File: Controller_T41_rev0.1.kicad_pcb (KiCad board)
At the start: 2 copper layers, 79 x 119.8 mm, 19 parts, among them J1 RJ45_LED_Shielded_x2, J2 RJ45_LED_Shielded_x2, J3 RJ45_LED_Shielded_x2, J4 RJ45_LED_Shielded_x2, J9 Screw_Terminal_01x02, U1 74HC245, U2 74HC245, U3 Teensy4.1, U4 74HC245, U5 74HC245

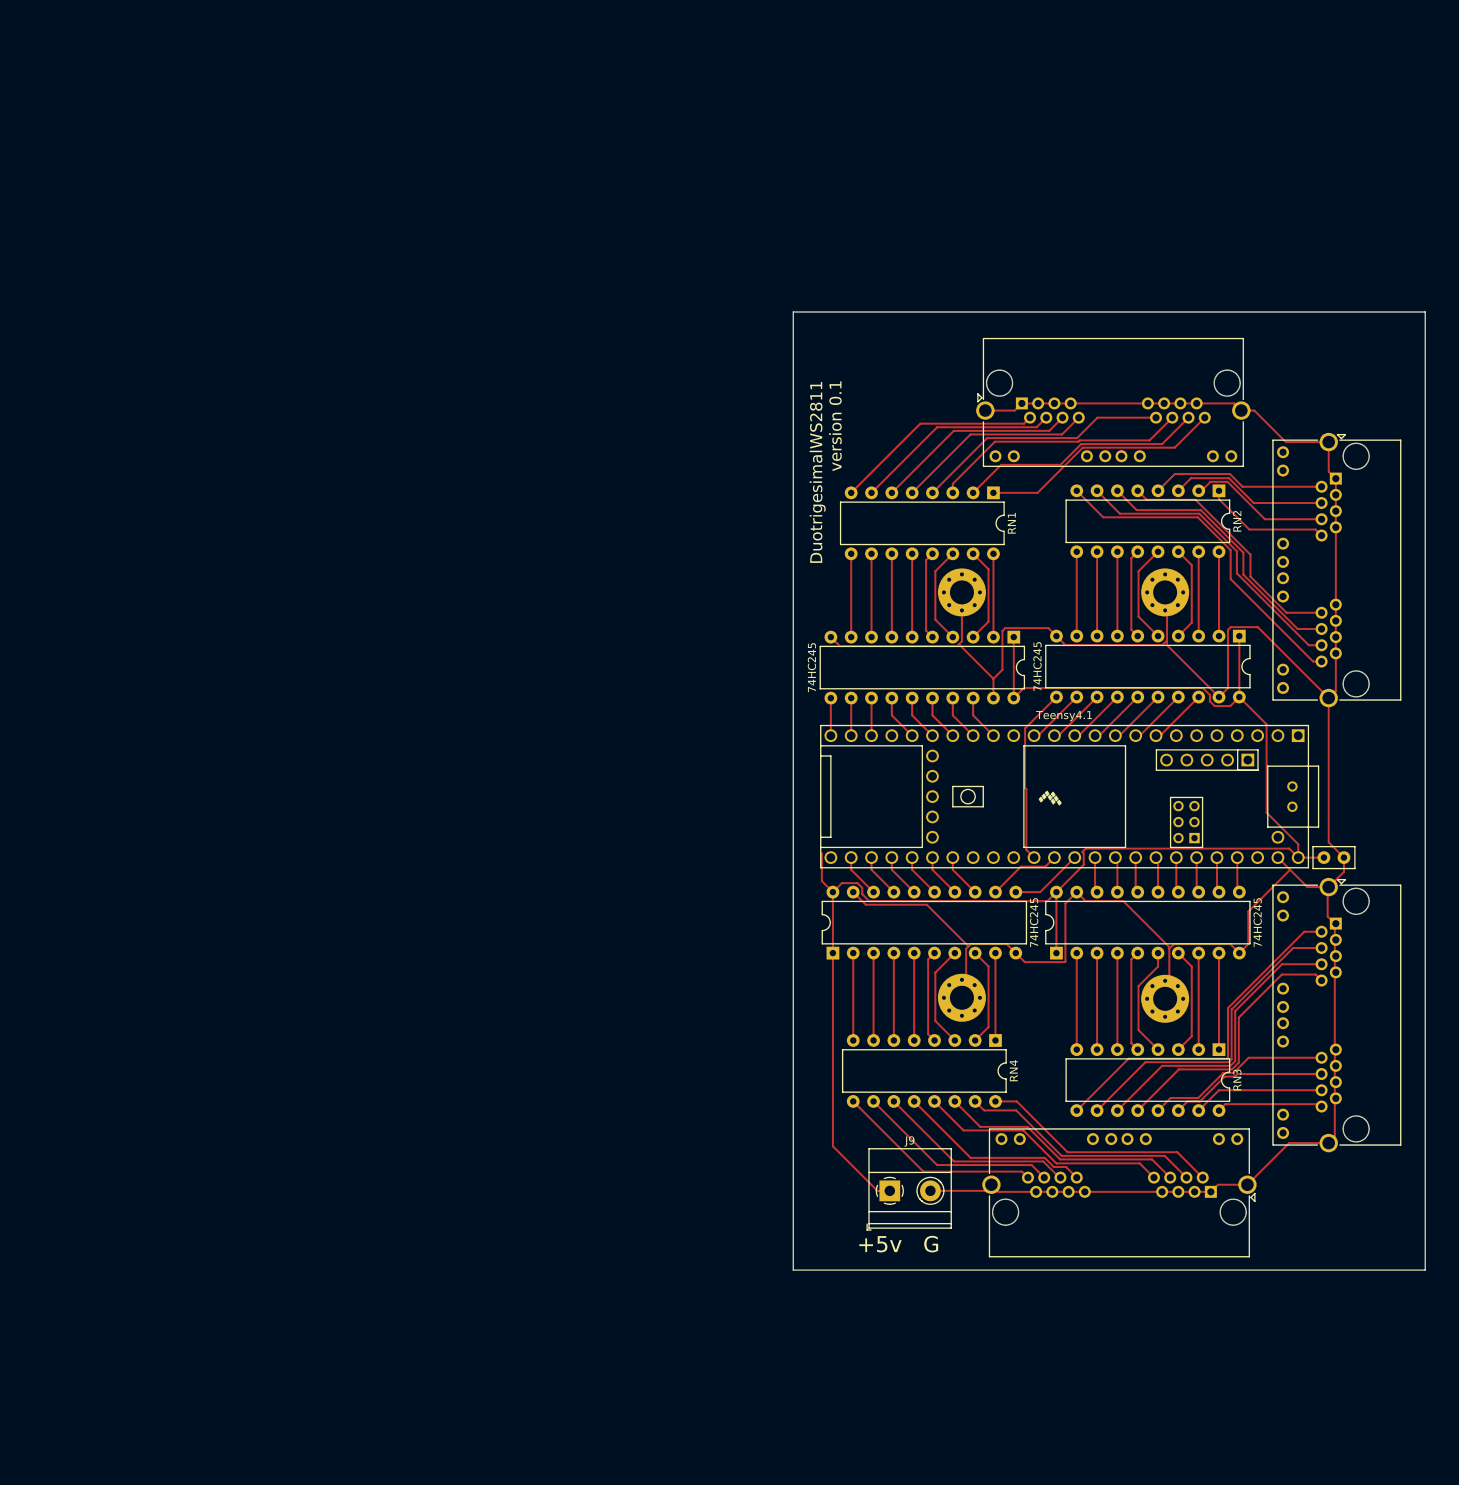
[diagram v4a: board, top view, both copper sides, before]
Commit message: Switching to SMT components where possible
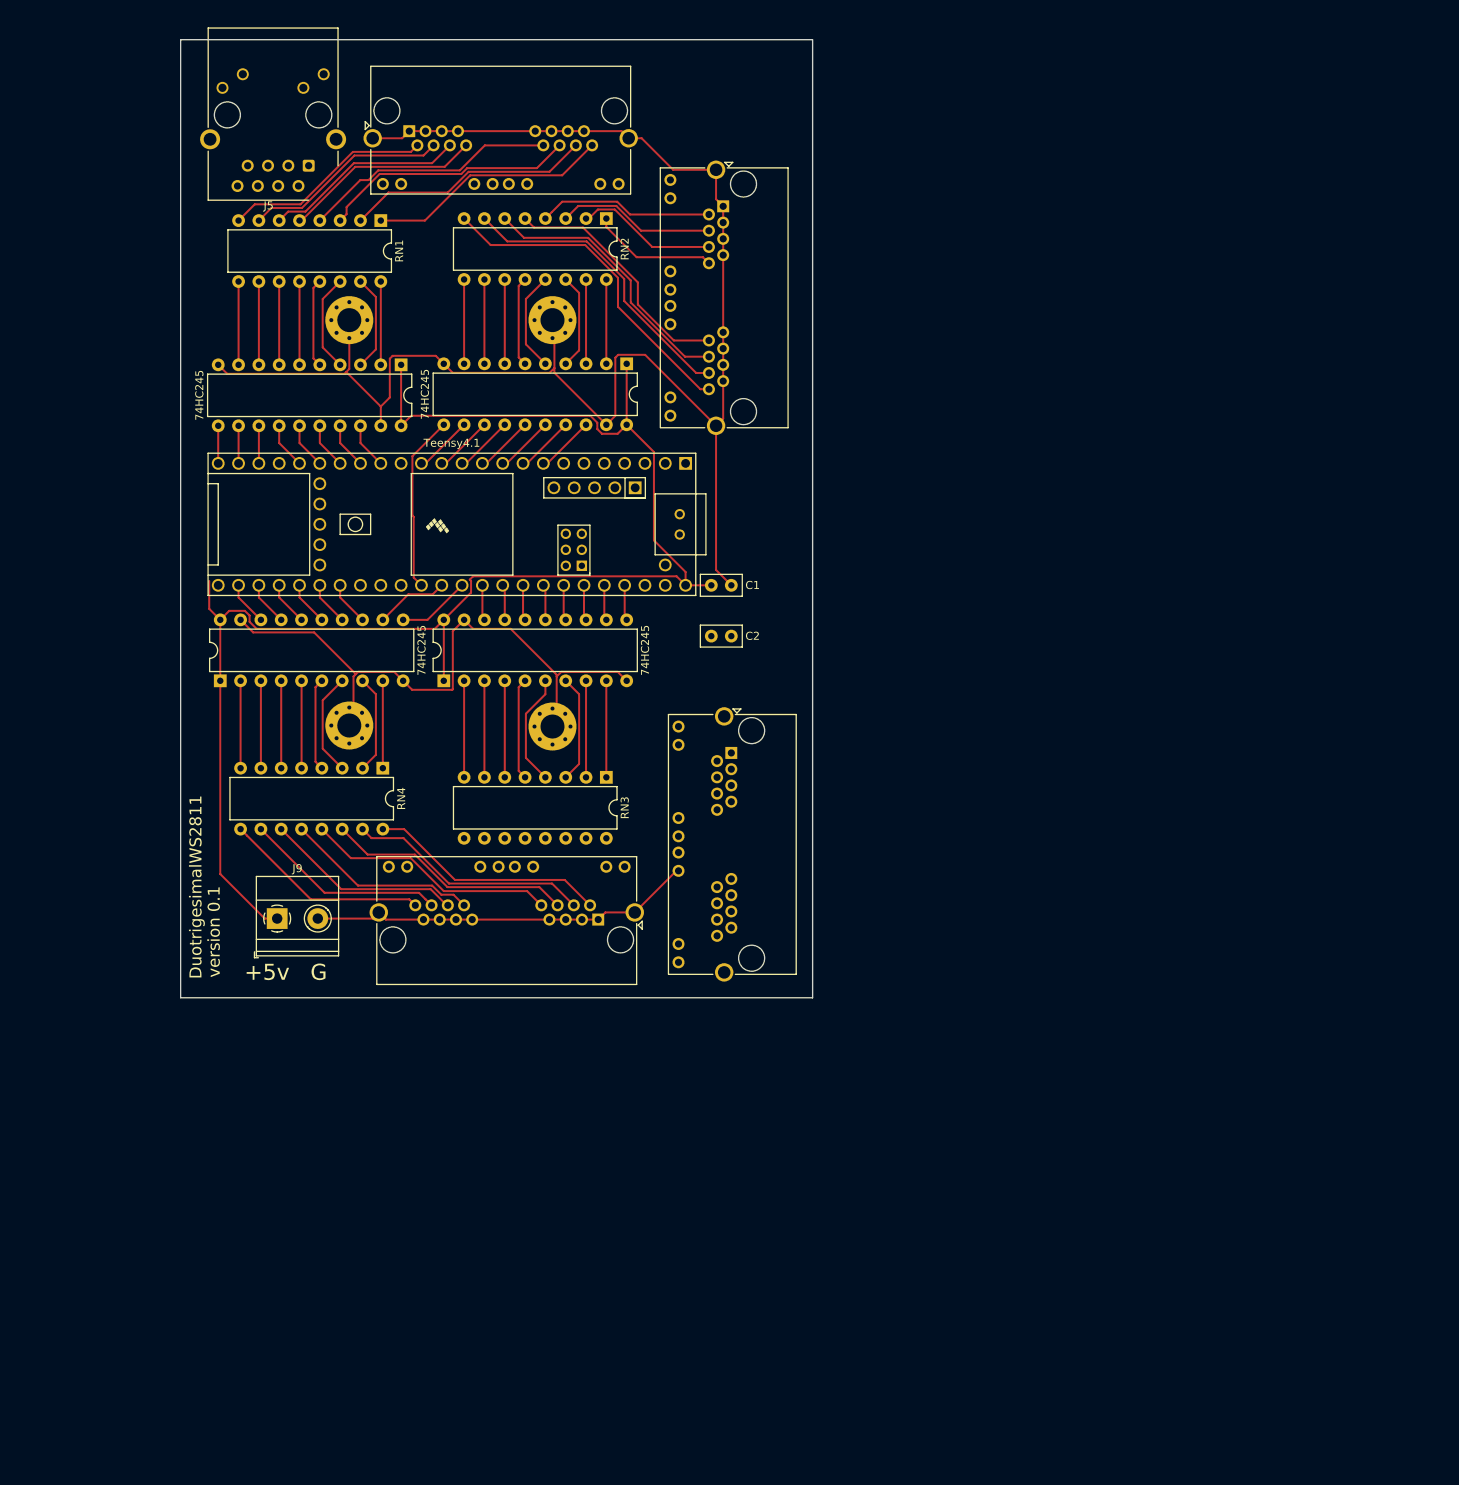
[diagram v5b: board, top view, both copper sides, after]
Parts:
- added C2: 0.1uF, Capacitor_THT:C_Disc_D5.0mm_W2.5mm_P2.50mm, F.Cu at (114.4, 102.9)
- added J5: RJ45_LED, Connector_RJ:RJ45_Cetus_J1B1211CCD_Horizontal, F.Cu at (61.6, 44.1)
- C1: value C -> 1uF
- moved RN1 83.8 mm to (70.6, 50.9)
- moved C1 83.8 mm to (114.4, 96.5)
- moved H1 83.8 mm to (66.7, 63.4)
- moved H2 83.8 mm to (66.7, 114.0)
- moved H3 83.8 mm to (92.1, 63.4)
- moved H4 83.8 mm to (92.1, 114.2)
- moved J3 83.8 mm to (97.8, 138.3)
- moved J9 83.8 mm to (57.7, 138.2)
- moved RN2 83.8 mm to (98.8, 50.7)
- moved RN3 83.8 mm to (98.8, 120.5)
- moved RN4 83.8 mm to (70.9, 119.4)
- moved U1 83.8 mm to (73.2, 69.0)
- moved U3 83.8 mm to (79.5, 88.9)
- moved U4 83.8 mm to (78.5, 108.5)
- moved J1 83.8 mm to (113.4, 49.1)
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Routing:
- net GND: track 387.8 -> 324.9 mm
- net Net-(J4-Pad2): track 43.5 -> 0.00 mm
- net Net-(J4-Pad4): track 40.1 -> 0.00 mm
- net Net-(J4-Pad6): track 36.8 -> 0.00 mm
- net Net-(J4-Pad8): track 33.6 -> 0.00 mm
- net Net-(J4-Pad14): track 23.2 -> 0.00 mm
- net Net-(J4-Pad16): track 19.8 -> 0.00 mm
- net Net-(J4-Pad18): track 16.4 -> 0.00 mm
- net Net-(J4-Pad20): track 13.3 -> 0.00 mm
